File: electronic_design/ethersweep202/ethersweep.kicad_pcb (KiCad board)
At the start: 2 copper layers, 79 x 38 mm, 89 parts, among them J1 AVR-ISP-6, J10 HR911105A, J2 Conn_01x02_Male, J3 Conn_01x04_Female, J4 Conn_01x02_Male, J5 Conn_01x02_Male, J6 Conn_01x07_Female, J7 Conn_01x07_Male, J8 AVR-ISP-6, M1 Stepper_Motor_bipolar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

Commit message: design and layout changes
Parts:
- moved R9 51.8 mm to (136.9, 91.7)
- moved R10 47.4 mm to (134.0, 91.5)
- moved R23 40.6 mm to (118.2, 92.0)
- moved R18 40.2 mm to (138.6, 85.6)
- moved C13 35.1 mm to (119.2, 93.9), turned to 90 degrees
- moved C7 30.9 mm to (135.2, 87.0)
- moved R21 16.8 mm to (116.4, 106.6), turned to 0 degrees
- moved Y2 15.2 mm to (113.8, 109.8)
- moved C33 15.2 mm to (111.9, 107.9)
- moved C34 15.2 mm to (116.5, 110.9)
- moved R4 2.75 mm to (137.0, 98.8)
- moved R7 2.75 mm to (131.0, 98.8)
- moved R5 2.45 mm to (135.0, 98.0)
- moved R6 2.45 mm to (133.0, 98.0)
- moved U6 2.16 mm to (132.5, 105.7)
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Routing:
- net Net-(R7-Pad2): track 3.20 -> 3.84 mm
- net Net-(R6-Pad2): track 3.03 -> 2.43 mm
- net Net-(R5-Pad2): track 3.02 -> 2.42 mm

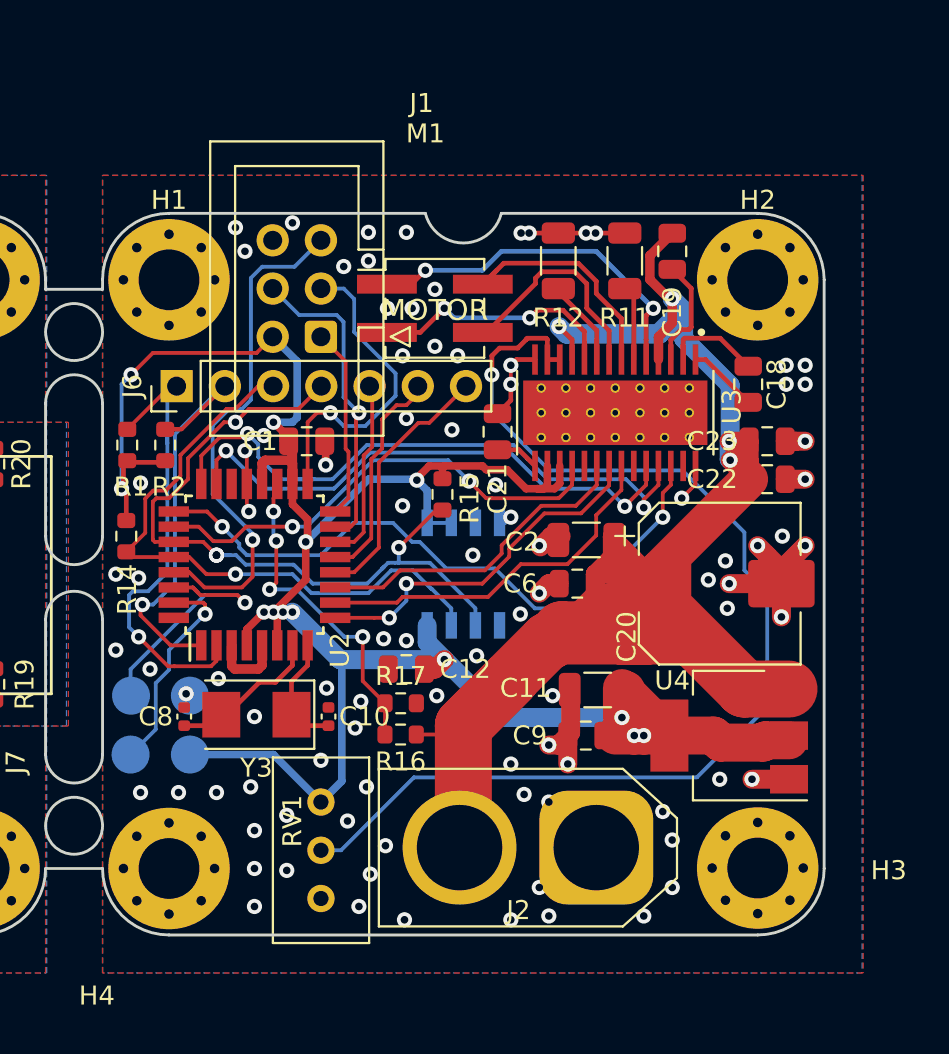
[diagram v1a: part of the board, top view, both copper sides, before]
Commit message: major power supply canges
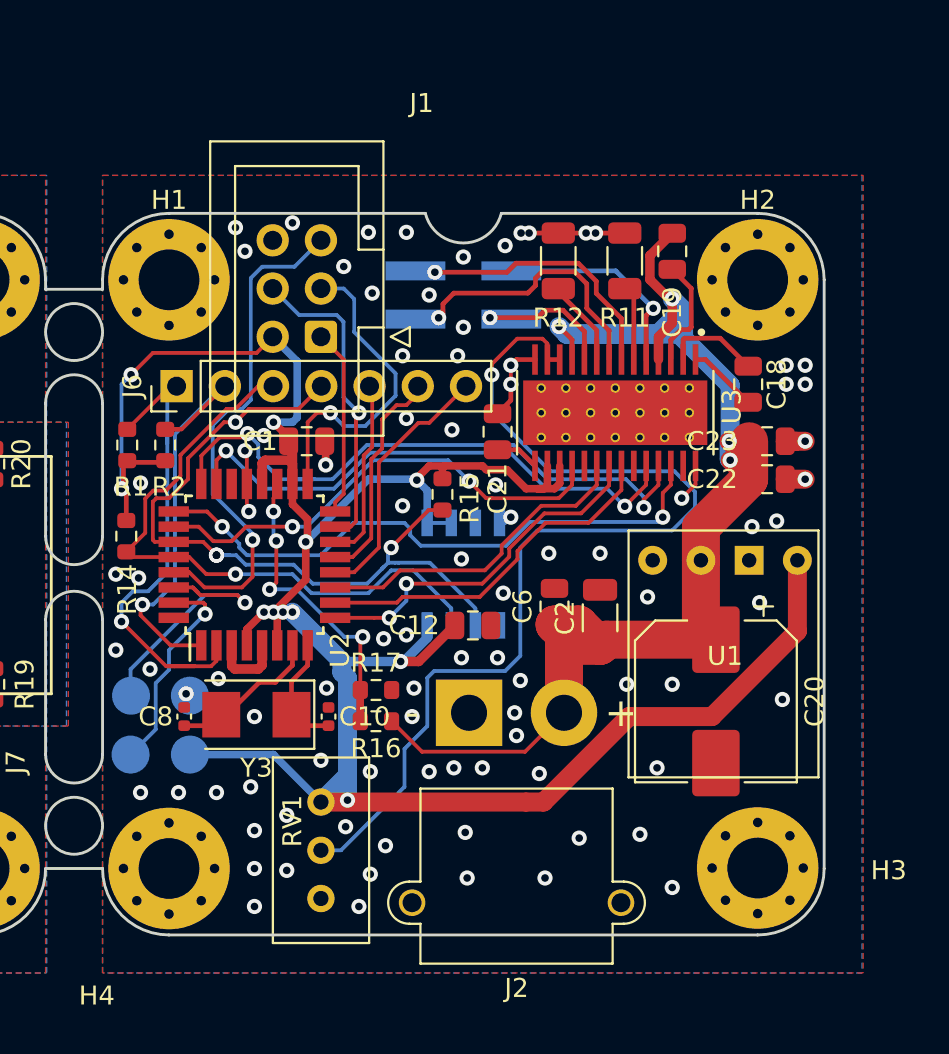
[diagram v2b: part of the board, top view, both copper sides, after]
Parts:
- removed C11: C4.7uF, Capacitor_SMD:C_1206_3216Metric
- removed C9: C100nF, Capacitor_SMD:C_0805_2012Metric
- removed U4: AMS1117-3.3, Package_TO_SOT_SMD:SOT-223-3_TabPin2
- added U1: Pololu_D24V3F3, Module:Pololu_D24V3F3, F.Cu at (191.2, 110.7)
- J2: footprint Connector_AMASS:AMASS_XT60-M_1x02_P7.20mm_Vertical -> Connector_AMASS:AMASS_XT30PW-M_1x02_P2.50mm_Horizontal
- M1: moved to B.Cu
- moved J2 9.76 mm to (182.8, 107.3)
- moved C20 6.20 mm to (195.8, 106.7), turned to 270 degrees
- moved C12 4.19 mm to (183.0, 102.7), turned to 180 degrees
- moved C2 4.16 mm to (189.7, 102.3), turned to 90 degrees
- moved C6 1.70 mm to (187.3, 101.7), turned to 90 degrees
- moved M1 1.66 mm to (182.5, 85.3), turned to 180 degrees
- moved R17 1.48 mm to (177.9, 106.1)
- moved R16 1.48 mm to (177.9, 107.7)
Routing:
- net +12V: track 122.2 -> 89.2 mm
- net GND: track 51.7 -> 31.8 mm, vias 98 -> 95
- net Net-(M1-Pad1): track 18.8 -> 11.1 mm, vias 2 -> 1
- net +3V3: track 136.2 -> 143.0 mm, vias 13 -> 11
- net Net-(RV1-Pad2): track 60.3 -> 54.1 mm
- net Net-(M1-Pad3): track 14.1 -> 7.97 mm, vias 2 -> 1
- net M2: track 34.3 -> 31.7 mm
- net Net-(M1-Pad4): track 11.7 -> 14.1 mm, vias 0 -> 1
- net ESTOP: track 25.3 -> 27.2 mm
- net Net-(M1-Pad2): track 12.5 -> 14.0 mm, vias 0 -> 1
- net voltage_detect: track 17.5 -> 16.3 mm
- net SDA: track 39.1 -> 39.9 mm
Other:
- board text added: "by Neumi 2021-03-24"
- board text added: "vers. 2.2.1"
- board text removed: "by Neumi 2021-02-10"
- board text removed: "vers. 2.0.1"

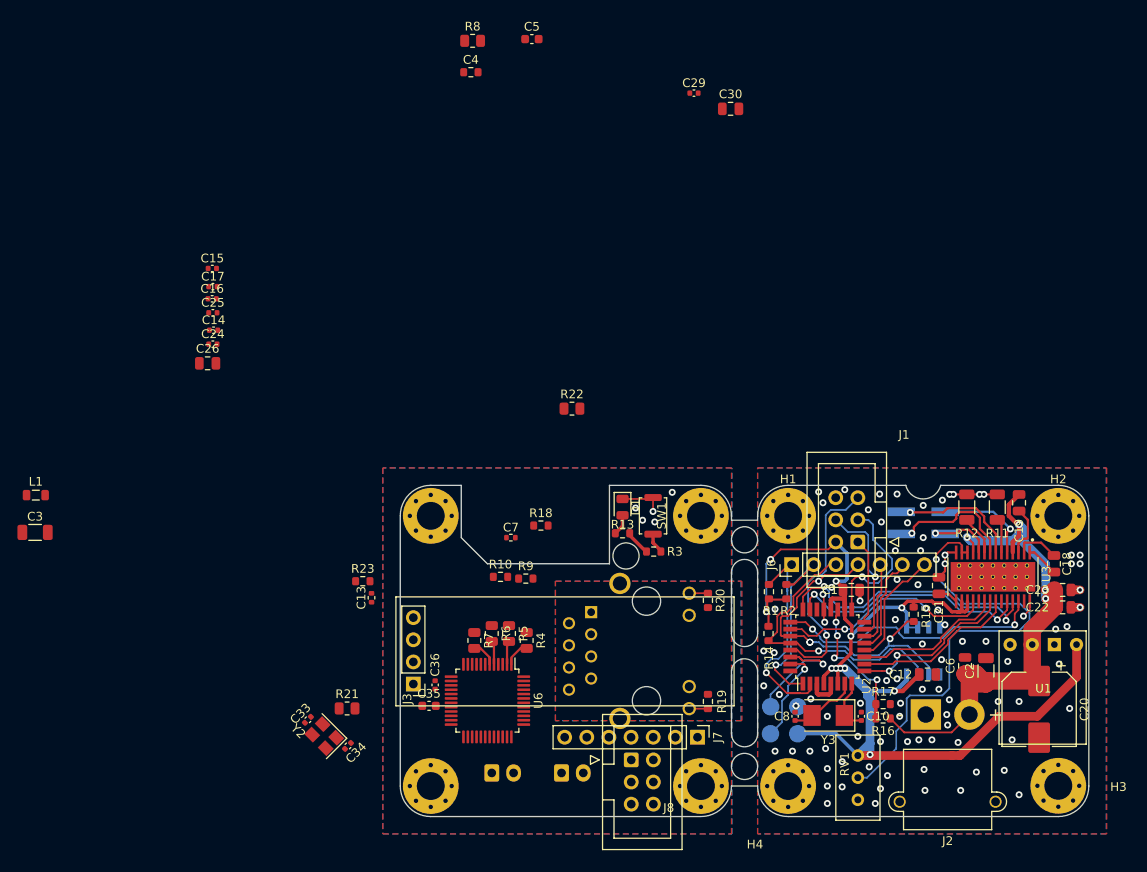
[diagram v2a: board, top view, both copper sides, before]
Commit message: layout changes, added status led ...
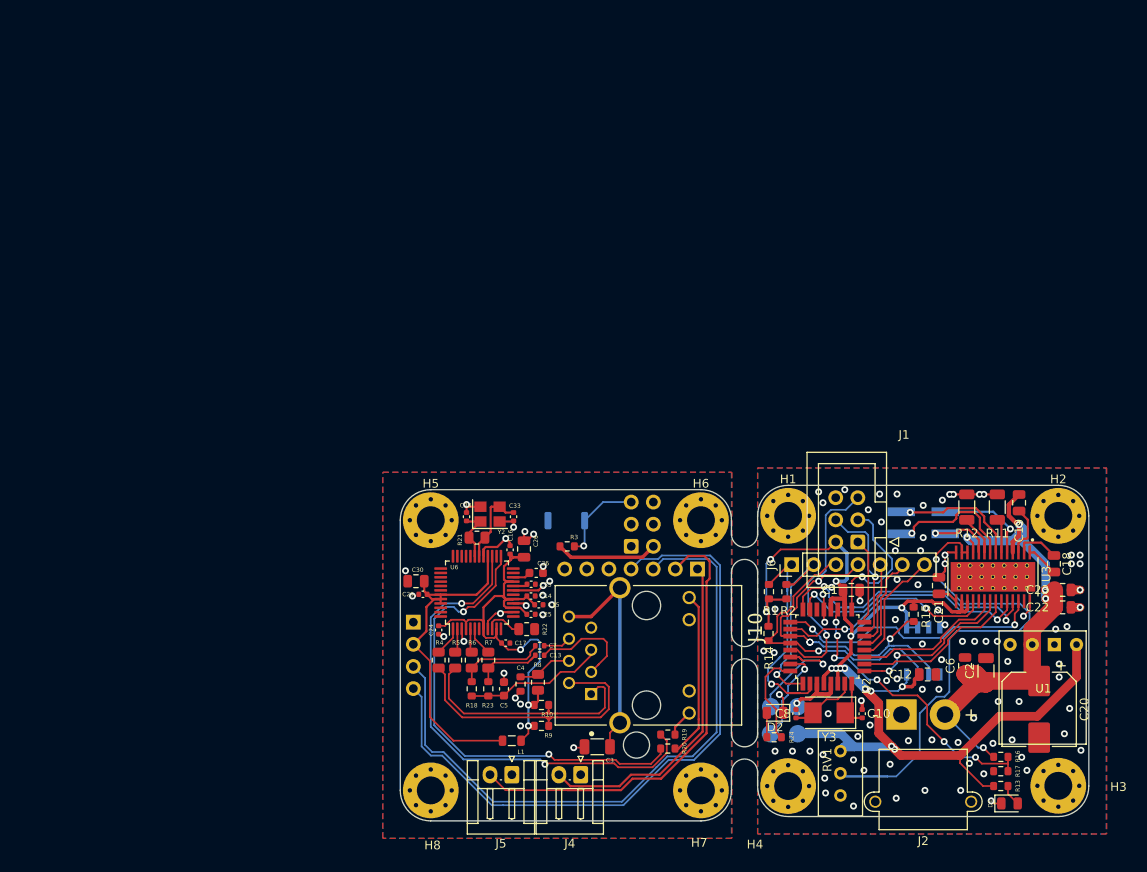
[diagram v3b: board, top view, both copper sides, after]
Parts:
- added D2: LED, LED_SMD:LED_0805_2012Metric, F.Cu at (165.5, 107.1)
- added R24: R330, Resistor_SMD:R_0603_1608Metric, F.Cu at (165.4, 109.9)
- H5, H6, H7, H8, J10, J4, J5: moved to F.Cu
- J3, J7, J8, SW1: moved to B.Cu
- moved C5 74.6 mm to (134.4, 104.3), turned to 270 degrees
- moved R8 74.0 mm to (138.3, 103.6), turned to 90 degrees
- moved C4 70.4 mm to (136.3, 103.8), turned to 90 degrees
- moved C3 69.0 mm to (145.1, 111.0), turned to 180 degrees
- moved C29 65.4 mm to (125.1, 93.5), turned to 180 degrees
- moved C30 65.1 mm to (124.3, 92.0), turned to 180 degrees
- moved L1 61.5 mm to (135.3, 110.3)
- moved D1 55.9 mm to (192.4, 117.5), turned to 0 degrees
- moved C15 53.8 mm to (138.4, 94.7)
- moved C17 52.9 mm to (134.6, 99.1)
- moved R13 52.2 mm to (191.4, 115.5), turned to 0 degrees
- moved C25 50.3 mm to (137.5, 95.8)
- moved C14 47.5 mm to (137.5, 93.7)
- moved C16 44.7 mm to (135.1, 88.4), turned to 90 degrees
- moved C26 42.1 mm to (136.7, 88.3), turned to 90 degrees
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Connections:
- U6 pad 11: +3V3 -> +3.3VA
- U6 pad 15: +3V3 -> +3.3VA
- U6 pad 17: +3V3 -> +3.3VA
- U6 pad 21: +3V3 -> +3.3VA
- U6 pad 4: +3V3 -> +3.3VA
- U6 pad 8: +3V3 -> +3.3VA
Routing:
- net SDA: track 39.9 -> 118.0 mm
- net SCL: track 33.3 -> 109.4 mm
- net +3.3VA: track 0.00 -> 62.3 mm, vias 0 -> 3
- net +3V3: track 143.0 -> 204.1 mm, vias 11 -> 14
- net Net-(R20-Pad2): track 0.00 -> 56.6 mm, vias 0 -> 2
- net Net-(R19-Pad2): track 0.00 -> 54.2 mm, vias 0 -> 2
- net ENDSTOP: track 23.7 -> 75.9 mm
- net ESTOP: track 27.2 -> 65.7 mm
- net GND: track 31.8 -> 67.1 mm, vias 95 -> 110
- net TD-: track 0.00 -> 33.2 mm
- net TD+: track 0.00 -> 29.7 mm
- net GND1: track 0.00 -> 26.7 mm
- net voltage_detect: track 16.3 -> 34.0 mm, vias 4 -> 6
- net ETHERNET_LED_A: track 2.15 -> 19.1 mm
- net RC: track 0.00 -> 16.4 mm
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- removed copper zone on B.Cu, net GND1
- removed copper zone on F.Cu, net GND1
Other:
- board size 79 x 38 mm -> 79 x 38.5 mm

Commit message: layout changes
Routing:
- net RST_ETHERNET: track 11.7 -> 31.2 mm, vias 0 -> 1
- net ETH_INT: track 13.6 -> 32.1 mm, vias 0 -> 1
- net SCK: track 17.6 -> 20.6 mm, vias 1 -> 2
- net MISO: track 9.88 -> 12.7 mm, vias 0 -> 1
- net CS_ETHERNET: track 9.85 -> 12.2 mm, vias 0 -> 1
- net MOSI: track 17.4 -> 19.3 mm, vias 1 -> 2
- net GND: track 67.1 -> 66.2 mm, vias 110 -> 109
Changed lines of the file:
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@@
     (thickness 1.6)
     (drawings 47)
-    (tracks 1182)
+    (tracks 1220)
     (zones 0)
     (modules 89)
@@
   )
   (setup
-    (last_trace_width 0.25)
+    (last_trace_width 0.2)
     (user_trace_width 0.2)
     (user_trace_width 0.4)
@@
   (segment (start 136.7 87.35) (end 137.05 87.35) (width 0.25) (layer F.Cu) (net 1))
   (segment (start 135.5 85.8) (end 135.5 85.08) (width 0.25) (layer F.Cu) (net 1))
-  (via (at 138.9 90.3) (size 0.8) (drill 0.4) (layers F.Cu B.Cu) (net 1))
-  (segment (start 138.875 90.325) (end 138.9 90.3) (width 0.25) (layer F.Cu) (net 1))
-  (segment (start 138.875 91.2) (end 138.875 90.325) (width 0.25) (layer F.Cu) (net 1))
   (segment (start 133.62501 88.07499) (end 134.6 87.1) (width 0.25) (layer F.Cu) (net 1))
   (segment (start 132.05 88.334298) (end 132.309308 88.07499) (width 0.25) (layer F.Cu) (net 1))
@@
   (segment (start 175.75 96.225) (end 176.200001 95.774999) (width 0.2) (layer F.Cu) (net 13))
   (segment (start 175.75 96.7) (end 175.75 96.225) (width 0.2) (layer F.Cu) (net 13))
+  (segment (start 130.3 91.55) (end 130.3 91.6) (width 0.25) (layer F.Cu) (net 13))
+  (via (at 130.3 91.55) (size 0.8) (drill 0.4) (layers F.Cu B.Cu) (net 13))
+  (segment (start 130.3 90.813998) (end 130.3 91.55) (width 0.2) (layer F.Cu) (net 13))
+  (segment (start 129.55 90.063998) (end 130.3 90.813998) (width 0.2) (layer F.Cu) (net 13))
+  (segment (start 129.55 89.1375) (end 129.55 90.063998) (width 0.2) (layer F.Cu) (net 13))
   (segment (start 174.5 95.05) (end 174.3 95.25) (width 0.2) (layer F.Cu) (net 14))
   (segment (start 148.839999 85.299999) (end 149 85.46) (width 0.2) (layer F.Cu) (net 14))
@@
   (segment (start 174.797166 91.5) (end 175.5 91.5) (width 0.2) (layer F.Cu) (net 14))
   (segment (start 174.3 91.997166) (end 174.797166 91.5) (width 0.2) (layer F.Cu) (net 14))
+  (segment (start 130.05 89.998299) (end 131.5 91.448299) (width 0.2) (layer F.Cu) (net 14))
+  (segment (start 130.05 89.1375) (end 130.05 89.998299) (width 0.2) (layer F.Cu) (net 14))
+  (segment (start 131.5 91.448299) (end 131.5 91.55) (width 0.2) (layer F.Cu) (net 14))
+  (segment (start 131.5 91.55) (end 131.5 91.55) (width 0.2) (layer F.Cu) (net 14))
+  (via (at 131.5 91.55) (size 0.8) (drill 0.4) (layers F.Cu B.Cu) (net 14))
   (segment (start 171.907999 83.809999) (end 171.309999 84.407999) (width 0.2) (layer B.Cu) (net 15))
   (segment (start 173.610001 83.809999) (end 171.907999 83.809999) (width 0.2) (layer B.Cu) (net 15))
@@
   (segment (start 176.190001 86.712167) (end 176.190001 90.690001) (width 0.2) (layer B.Cu) (net 16))
   (segment (start 172.46 84.96) (end 173.84999 86.34999) (width 0.2) (layer B.Cu) (net 16))
+  (segment (start 129.35 90.9) (end 129.35 90.9) (width 0.25) (layer F.Cu) (net 16))
+  (via (at 129.35 90.9) (size 0.8) (drill 0.4) (layers F.Cu B.Cu) (net 16))
+  (segment (start 129.05 90.6) (end 129.35 90.9) (width 0.2) (layer F.Cu) (net 16))
+  (segment (start 129.05 89.1375) (end 129.05 90.6) (width 0.2) (layer F.Cu) (net 16))
   (segment (start 169.5 104.565002) (end 169.5 103.75) (width 0.2) (layer F.Cu) (net 17))
   (segment (start 169.215001 104.850001) (end 169.5 104.565002) (width 0.2) (layer F.Cu) (net 17))
@@
   (segment (start 177.700001 90.240001) (end 177.700001 93.299999) (width 0.2) (layer F.Cu) (net 21))
   (segment (start 177.56 90.1) (end 177.700001 90.240001) (width 0.2) (layer F.Cu) (net 21))
+  (segment (start 130.55 89.905346) (end 131.194654 90.55) (width 0.2) (layer F.Cu) (net 21))
+  (segment (start 130.55 89.1375) (end 130.55 89.905346) (width 0.2) (layer F.Cu) (net 21))
+  (segment (start 131.194654 90.55) (end 131.75 90.55) (width 0.2) (layer F.Cu) (net 21))
+  (segment (start 131.75 90.55) (end 131.85 90.55) (width 0.2) (layer F.Cu) (net 21))
+  (via (at 131.75 90.55) (size 0.8) (drill 0.4) (layers F.Cu B.Cu) (net 21))
   (segment (start 176.663998 99.1) (end 175.75 99.1) (width 0.2) (layer F.Cu) (net 22))
   (segment (start 177.650021 98.113977) (end 176.663998 99.1) (width 0.2) (layer F.Cu) (net 22))
@@
   (segment (start 179.500001 91.099999) (end 178.980001 91.099999) (width 0.2) (layer F.Cu) (net 22))
   (segment (start 180.1 90.1) (end 180.1 90.5) (width 0.2) (layer F.Cu) (net 22))
+  (segment (start 129 92.75) (end 129 92.75) (width 0.25) (layer F.Cu) (net 22))
+  (via (at 129 92.75) (size 0.8) (drill 0.4) (layers F.Cu B.Cu) (net 22))
+  (segment (start 127.905346 90.55) (end 127.1375 90.55) (width 0.2) (layer F.Cu) (net 22))
+  (segment (start 129 91.644654) (end 127.905346 90.55) (width 0.2) (layer F.Cu) (net 22))
+  (segment (start 129 92.75) (end 129 91.644654) (width 0.2) (layer F.Cu) (net 22))
+  (segment (start 142.749999 91.750001) (end 143.9 90.6) (width 0.2) (layer B.Cu) (net 22))
+  (segment (start 140.357998 91.3) (end 140.807999 91.750001) (width 0.2) (layer B.Cu) (net 22))
+  (segment (start 140.807999 91.750001) (end 142.749999 91.750001) (width 0.2) (layer B.Cu) (net 22))
+  (segment (start 139.063998 91.3) (end 140.357998 91.3) (width 0.2) (layer B.Cu) (net 22))
+  (segment (start 137.613998 92.75) (end 139.063998 91.3) (width 0.2) (layer B.Cu) (net 22))
+  (segment (start 129 92.75) (end 137.613998 92.75) (width 0.2) (layer B.Cu) (net 22))
   (segment (start 169.57 107.68) (end 169.85 107.4) (width 0.25) (layer F.Cu) (net 26))
   (segment (start 169.27 107.68) (end 167.9 107.68) (width 0.25) (layer F.Cu) (net 26))
@@
   (segment (start 180.132849 92.032849) (end 180.707151 92.032849) (width 0.2) (layer F.Cu) (net 70))
   (segment (start 175.75 99.9) (end 176.75 99.9) (width 0.2) (layer F.Cu) (net 70))
+  (segment (start 127.3 89.25) (end 127.3 89.25) (width 0.25) (layer F.Cu) (net 70))
+  (via (at 127.3 89.25) (size 0.8) (drill 0.4) (layers F.Cu B.Cu) (net 70))
+  (segment (start 127.4125 89.1375) (end 127.3 89.25) (width 0.2) (layer F.Cu) (net 70))
+  (segment (start 128.55 89.1375) (end 127.4125 89.1375) (width 0.2) (layer F.Cu) (net 70))
+  (segment (start 139.1983 90.6) (end 141.36 90.6) (width 0.2) (layer B.Cu) (net 70))
+  (segment (start 129.036002 91.75) (end 129.635992 92.34999) (width 0.2) (layer B.Cu) (net 70))
+  (segment (start 137.44831 92.34999) (end 139.1983 90.6) (width 0.2) (layer B.Cu) (net 70))
+  (segment (start 127.3 89.25) (end 127.3 91.2) (width 0.2) (layer B.Cu) (net 70))
+  (segment (start 129.635992 92.34999) (end 137.44831 92.34999) (width 0.2) (layer B.Cu) (net 70))
+  (segment (start 127.85 91.75) (end 129.036002 91.75) (width 0.2) (layer B.Cu) (net 70))
+  (segment (start 127.3 91.2) (end 127.85 91.75) (width 0.2) (layer B.Cu) (net 70))
   (segment (start 138.0125 102.975) (end 138.3 102.6875) (width 0.2) (layer F.Cu) (net 71))
   (segment (start 136.3 102.975) (end 138.0125 102.975) (width 0.2) (layer F.Cu) (net 71))

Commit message: layout done. EMI improvements
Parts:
- moved R3 3.95 mm to (141.5, 84.0)
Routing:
- net MOSI: track 19.3 -> 45.0 mm
- net SCK: track 20.6 -> 43.2 mm
- net MISO: track 12.7 -> 33.9 mm, vias 1 -> 2
- net CS_ETHERNET: track 12.2 -> 29.0 mm
- net +3V3: track 204.1 -> 219.3 mm, vias 14 -> 17
- net rst: track 37.3 -> 40.4 mm, vias 2 -> 1
- net ETH_INT: track 32.1 -> 34.6 mm
- net ESTOP: track 65.7 -> 68.1 mm
- net RST_ETHERNET: track 31.2 -> 33.5 mm
- net GND: vias 109 -> 192
- net (no net): vias 0 -> 1
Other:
- board text added: "by Neumi 2021-03-30"
- board text removed: "by Neumi 2021-03-24"
